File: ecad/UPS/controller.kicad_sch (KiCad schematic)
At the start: 45 parts, among them J10 BOARD_10K_NTC, J4 PROG, J7 Fan_Connector, J9 OLED_3V3_I2C2, Q8 2N7002, U4 STM32L152RCT6, U5 AP2112K-3.3TRG1, U6 BOOT0, U7 NRST

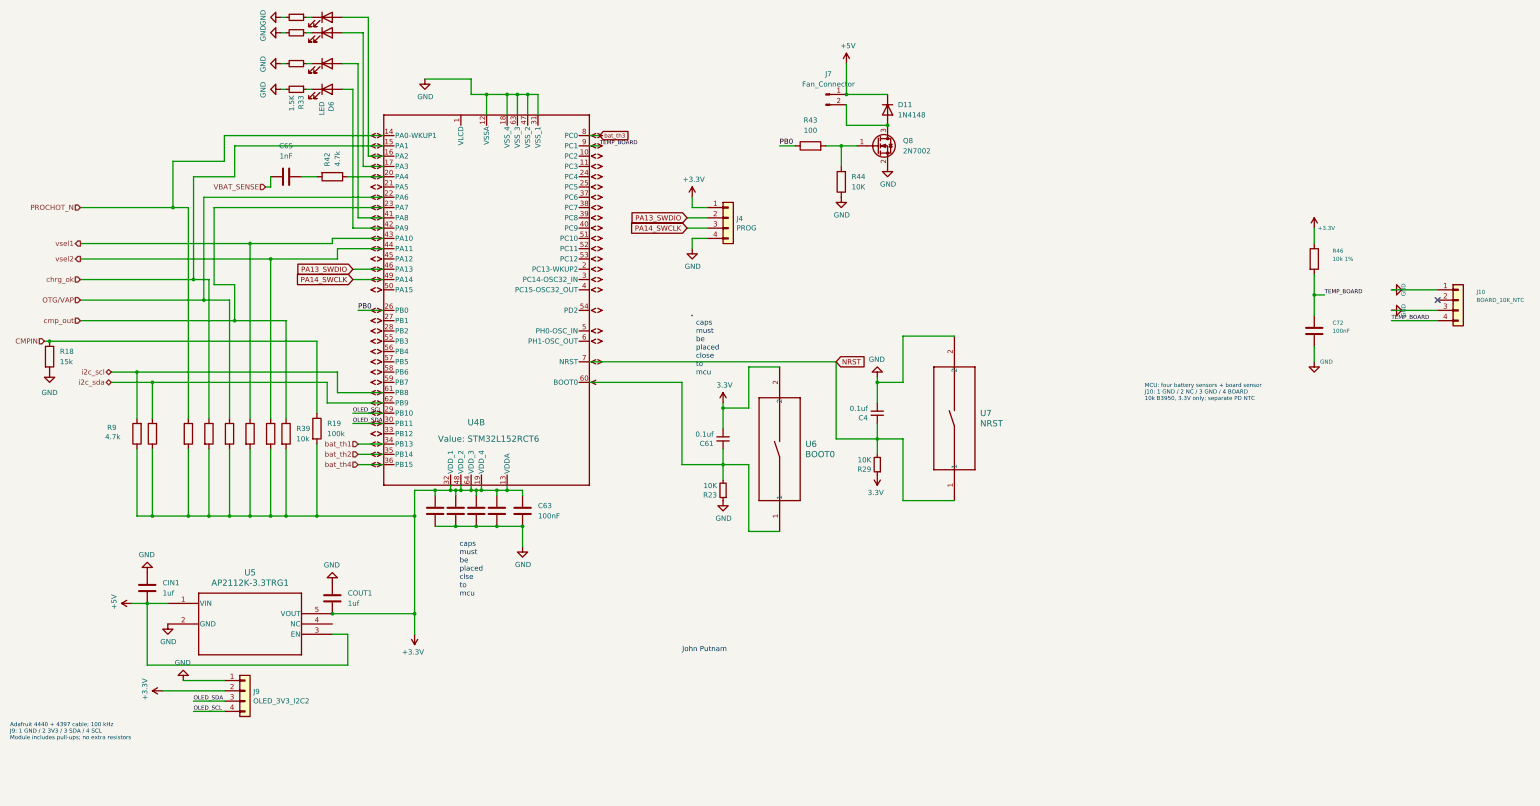
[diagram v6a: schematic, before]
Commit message: more stuff to route yay!
uart for the pi5
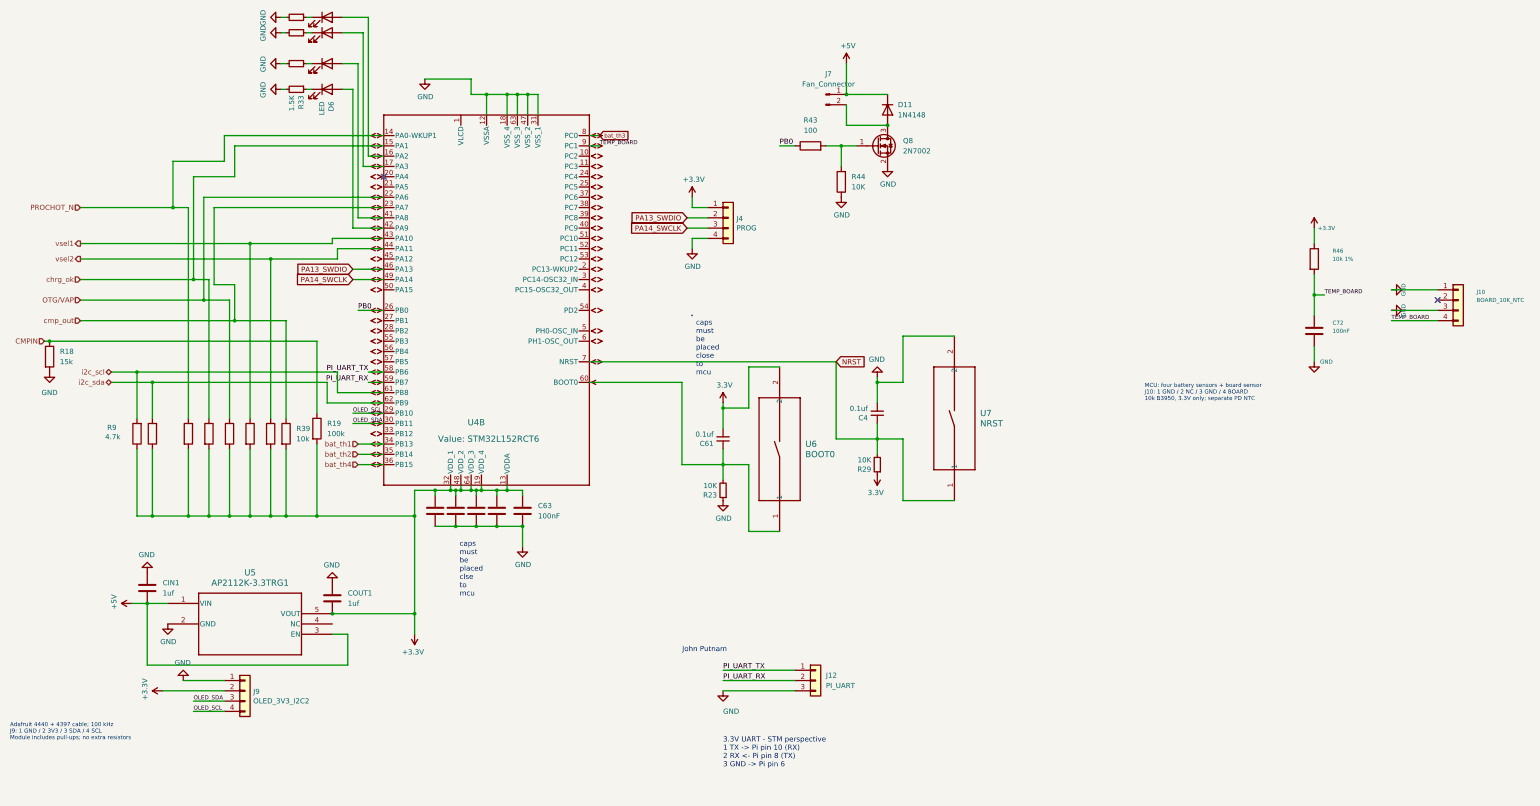
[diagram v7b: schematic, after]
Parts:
- removed C65: 1nF, Capacitor_SMD:C_0603_1608Metric_Pad1.08x0.95mm_HandSolder, symbol Device:C
- removed R42: 4.7k, Resistor_SMD:R_0805_2012Metric, symbol Device:R
- added J12: PI_UART, Connector_PinHeader_2.54mm:PinHeader_1x03_P2.54mm_Vertical, symbol Connector_Generic:Conn_01x03
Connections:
- net GND: now also J12.3 (Pin_3)
- net PI_UART_TX: now reaches U4.58 (PB6)
- net PI_UART_TX: now also J12.1 (Pin_1)
- net PI_UART_RX: now reaches U4.59 (PB7)
- net PI_UART_RX: now also J12.2 (Pin_2)
- no-connect marks 1 -> 2
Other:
- note added: "3.3V UART - STM perspective 1 TX -> Pi pin 10 (RX) 2 RX <- Pi pin 8 (TX) 3 GND -> Pi pin 6"
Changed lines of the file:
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@@
 	(wire
 		(pts
-			(xy 78.74 58.42) (xy 78.74 55.88)
-		)
-		(stroke
-			(width 0)
-			(type default)
-		)
-	)
-	(wire
-		(pts
 			(xy 228.6 120.65) (xy 228.6 124.46)
 		)
@@
 	(wire
 		(pts
-			(xy 97.79 55.88) (xy 106.68 55.88)
-		)
-		(stroke
-			(width 0)
-			(type default)
-		)
-	)
-	(wire
-		(pts
 			(xy 219.71 48.26) (xy 219.71 53.34)
 		)
@@
 	(wire
 		(pts
-			(xy 86.36 55.88) (xy 90.17 55.88)
-		)
-		(stroke
-			(width 0)
-			(type default)
-		)
-	)
-	(wire
-		(pts
 			(xy 218.44 120.65) (xy 228.6 120.65)
 		)
@@
 	(wire
 		(pts
-			(xy 77.47 58.42) (xy 78.74 58.42)
-		)
-		(stroke
-			(width 0)
-			(type default)
-		)
-	)
-	(wire
-		(pts
 			(xy 119.38 133.35) (xy 119.38 134.62)
 		)
@@
 		)
 	)
-	(hierarchical_label "VBAT_SENSE"
-		(shape input)
-		(at 77.47 58.42 180)
-		(effects
-			(font
-				(size 1.27 1.27)
-			)
-			(justify right)
-		)
-	)
 	(hierarchical_label "chrg_ok"
 		(shape input)
@@
 	)
 	(symbol
-		(lib_id "Device:C")
-		(at 82.55 55.88 90)
-		(mirror x)
-		(unit 1)
-		(body_style 1)
-		(exclude_from_sim no)
-		(in_bom yes)
-		(on_board yes)
-		(in_pos_files yes)
-		(dnp no)
-		(fields_autoplaced yes)
-		(property "Reference" "C65"
-			(at 82.55 48.26 90)
-			(show_name no)
-			(do_not_autoplace no)
-			(effects
-				(font
-					(size 1.27 1.27)
-				)
-			)
-		)
-		(property "Value" "1nF"
-			(at 82.55 50.8 90)
-			(show_name no)
-			(do_not_autoplace no)
-			(effects
-				(font
-					(size 1.27 1.27)
-				)
-			)
-		)
-		(property "Footprint" "Capacitor_SMD:C_0603_1608Metric_Pad1.08x0.95mm_HandSolder"
-			(at 86.36 56.8452 0)
-			(hide yes)
-			(show_name no)
-			(do_not_autoplace no)
-			(effects
-				(font
-					(size 1.27 1.27)
-				)
-			)
-		)
-		(property "Datasheet" ""
-			(at 82.55 55.88 0)
-			(hide yes)
-			(show_name no)
-			(do_not_autoplace no)
-			(effects
-				(font
-					(size 1.27 1.27)
-				)
-			)
-		)
-		(property "Description" "Unpolarized capacitor"
-			(at 82.55 55.88 0)
-			(hide yes)
-			(show_name no)
-			(do_not_autoplace no)
-			(effects
-				(font
-					(size 1.27 1.27)
-				)
-			)
-		)
-		(pin "2"
-		)
-		(pin "1"
-		)
-		(instances
-			(project "controller"
-				(path "/50450634-21c9-467c-beaf-30f36150c371"
-					(reference "C10")
-					(unit 1)
-				)
-			)
-			(project "UPS"
-				(path "/9d92b60a-4a6b-449c-b462-cab19e69d38c/1d606685-c4fd-4b8c-9a71-b1626d28c437"
-					(reference "C65")
-					(unit 1)
-				)
-			)
-		)
-	)
-	(symbol
 		(lib_id "Device:R_Small")
 		(at 85.09 34.29 270)
@@
 		)
 	)
-	(symbol
-		(lib_id "Device:R")
-		(at 93.98 55.88 270)
-		(unit 1)
-		(body_style 1)
-		(exclude_from_sim no)
-		(in_bom yes)
-		(on_board yes)
-		(in_pos_files yes)
-		(dnp no)
-		(fields_autoplaced yes)
-		(property "Reference" "R42"
-			(at 92.7099 53.34 0)
-			(show_name no)
-			(do_not_autoplace no)
-			(effects
-				(font
-					(size 1.27 1.27)
-				)
-				(justify right)
-			)
-		)
-		(property "Value" "4.7k"
-			(at 95.2499 53.34 0)
-			(show_name no)
-			(do_not_autoplace no)
-			(effects
-				(font
-					(size 1.27 1.27)
-				)
-				(justify right)
-			)
-		)
-		(property "Footprint" "Resistor_SMD:R_0805_2012Metric"
-			(at 93.98 54.102 90)
-			(hide yes)
-			(show_name no)
-			(do_not_autoplace no)
-			(effects
-				(font
-					(size 1.27 1.27)
-				)
-			)
-		)
-		(property "Datasheet" ""
-			(at 93.98 55.88 0)
-			(hide yes)
-			(show_name no)
-			(do_not_autoplace no)
-			(effects
-				(font
-					(size 1.27 1.27)
-				)
-			)
-		)
-		(property "Description" "Resistor"
-			(at 93.98 55.88 0)
-			(hide yes)
-			(show_name no)
-			(do_not_autoplace no)
-			(effects
-				(font
-					(size 1.27 1.27)
-				)
-			)
-		)
-		(pin "1"
-		)
-		(pin "2"
-		)
-		(instances
-			(project "controller"
-				(path "/50450634-21c9-467c-beaf-30f36150c371"
-					(reference "R17")
-					(unit 1)
-				)
-			)
-			(project "UPS"
-				(path "/9d92b60a-4a6b-449c-b462-cab19e69d38c/1d606685-c4fd-4b8c-9a71-b1626d28c437"
-					(reference "R42")
-					(unit 1)
-				)
-			)
-		)
-	)
 	(sheet_instances
 		(path "/"
@@
 		)
 	)
+	(no_connect (at 106.68 55.88))
+(symbol (lib_id "Connector_Generic:Conn_01x03") (at 213.36 180.34 0) (unit 1) (in_bom yes) (on_board yes) (dnp no)
+(property "Reference" "J12" (at 215.9 179.07 0)  (effects (font (size 1.27 1.27)) (justify left)))
+(property "Value" "PI_UART" (at 215.9 181.61 0)  (effects (font (size 1.27 1.27)) (justify left)))
+(property "Footprint" "Connector_PinHeader_2.54mm:PinHeader_1x03_P2.54mm_Vertical" (at 213.36 180.34 0) (hide yes) (effects (font (size 1.27 1.27)) (justify left)))
+(pin "1")
+(pin "2")
+(pin "3")
+(instances (project "UPS" (path "/9d92b60a-4a6b-449c-b462-cab19e69d38c/1d606685-c4fd-4b8c-9a71-b1626d28c437" (reference "J12") (unit 1)))))
+(wire (pts (xy 106.68 104.14) (xy 102.87 104.14)) (stroke (width 0) (type default)))
+(label "PI_UART_TX" (at 102.87 104.14 0) (effects (font (size 1.27 1.27)) (justify right bottom)))
+(wire (pts (xy 208.28 177.8) (xy 190.5 177.8)) (stroke (width 0) (type default)))
+(label "PI_UART_TX" (at 190.5 177.8 0) (effects (font (size 1.27 1.27)) (justify left bottom)))
+(wire (pts (xy 106.68 106.68) (xy 102.87 106.68)) (stroke (width 0) (type default)))
+(label "PI_UART_RX" (at 102.87 106.68 0) (effects (font (size 1.27 1.27)) (justify right bottom)))
+(wire (pts (xy 208.28 180.34) (xy 190.5 180.34)) (stroke (width 0) (type default)))
+(label "PI_UART_RX" (at 190.5 180.34 0) (effects (font (size 1.27 1.27)) (justify left bottom)))
+(wire (pts (xy 208.28 182.88) (xy 190.5 182.88)) (stroke (width 0) (type default)))
+(symbol (lib_id "power:GND") (at 190.5 182.88 0) (unit 1) (in_bom yes) (on_board yes) (property "Reference" "#PWR0150" (at 190.5 189.23 0) (hide yes) (effects (font (size 1.27 1.27)) (justify left)))(property "Value" "GND" (at 190.5 187.96 0)  (effects (font (size 1.27 1.27)) (justify left))) (pin "1") (instances (project "UPS" (path "/9d92b60a-4a6b-449c-b462-cab19e69d38c/1d606685-c4fd-4b8c-9a71-b1626d28c437" (reference "#PWR0150") (unit 1)))))
+(text "3.3V UART - STM perspective\n1 TX -> Pi pin 10 (RX)\n2 RX <- Pi pin 8 (TX)\n3 GND -> Pi pin 6" (at 190.5 194.31 0) (effects (font (size 1.27 1.27)) (justify left top)))
 )

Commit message: Organize UPS placement for Pi 5 mounting and power-stage review
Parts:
- U6, U7: footprint B3U-1000P-B -> UPS:B3U-1000P-B
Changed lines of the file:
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@@
 			)
 		)
-		(property "Footprint" "B3U-1000P-B"
+		(property "Footprint" "UPS:B3U-1000P-B"
 			(at 247.65 135.89 0)
 			(hide yes)
@@
 			)
 		)
-		(property "Footprint" "B3U-1000P-B"
+		(property "Footprint" "UPS:B3U-1000P-B"
 			(at 204.47 143.51 0)
 			(hide yes)
